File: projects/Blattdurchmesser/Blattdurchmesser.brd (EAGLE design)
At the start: 100 x 80 mm, 14 parts, among them K1 TX2_RELAY", U1 ARDUINOR3-DIMENSION

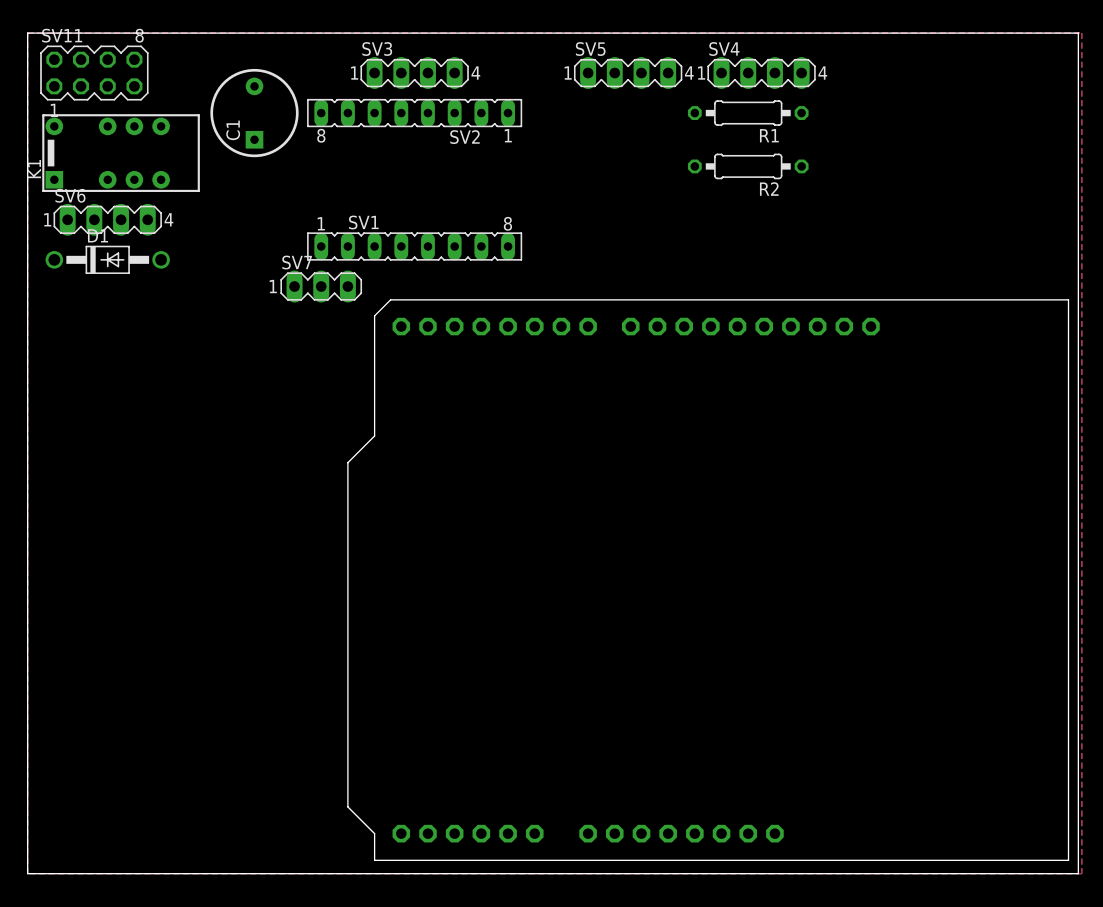
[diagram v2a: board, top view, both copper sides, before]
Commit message: improvement; * replace arduino part/footprint by one that does                not have milling slots              * avoid using a relais as it has disadvantages
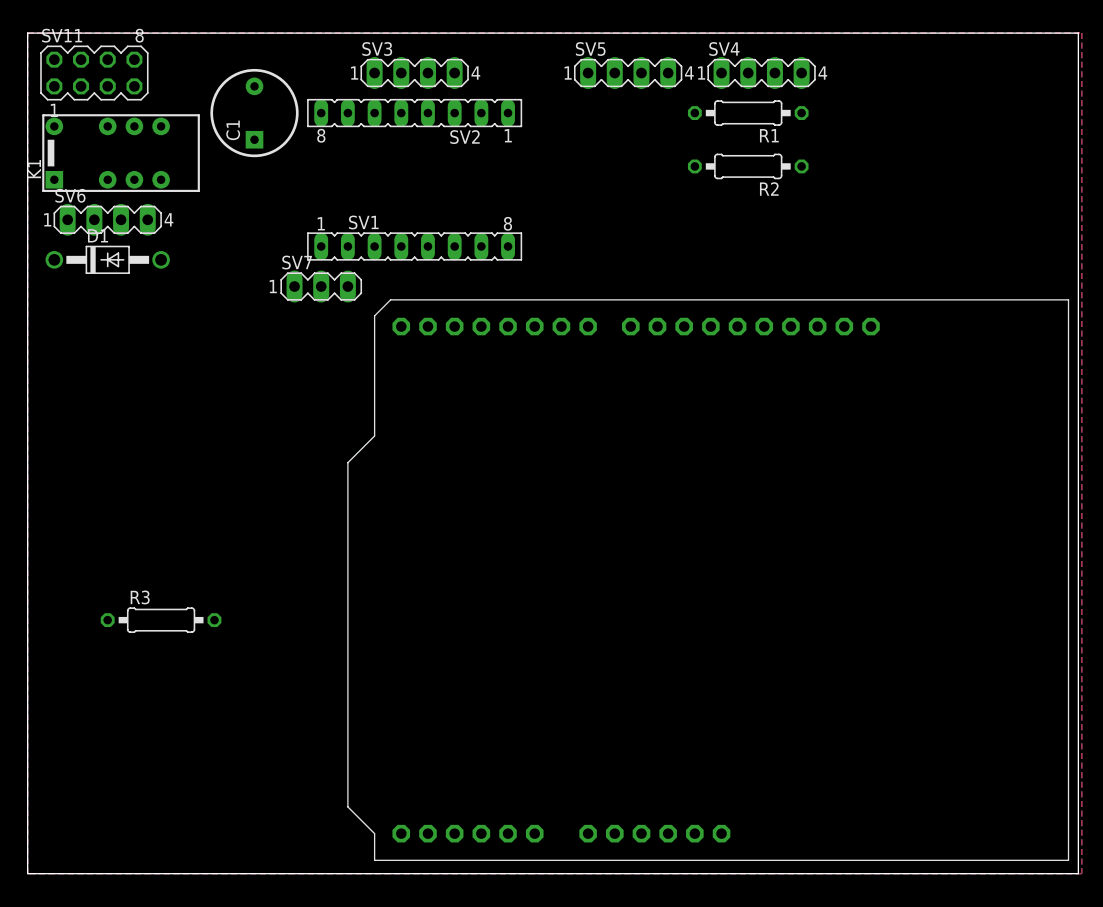
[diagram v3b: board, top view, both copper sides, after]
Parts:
- removed U1: ARDUINOR3-DIMENSION, adafruit:ARDUINOR3
- added Q1: ARDUINOR3-NOIOREF-NOTEXT, adafruit:ARDUINOR3-NOTEXT-NOIOREF
- added R3: ?, rcl:0207/10
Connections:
- removed net N$10: K1.4, SV1.1, SV7.2
- new net N$16: D1.C, K1.1
- new net N$8: D1.A, K1.12
- net +12V: no longer D1.C, K1.1
- net +5V: now also Q1.5V, R3.2; no longer K1.3, U1.5V
- net 3V: now also Q1.3V; no longer U1.3V
- net GND: now also Q1.GND; no longer SV6.1, U1.GND
- net GND1: now also Q1.GND1; no longer U1.GND1
- net GND2: now also Q1.GND2; no longer U1.GND2
- net N$1: now also Q1.D4; no longer U1.D4
- net N$11: now also Q1.D12, SV6.1; no longer D1.A, K1.12, SV6.2
- net N$12: now also Q1.D10; no longer U1.D10
- net N$13: now also Q1.D9; no longer U1.D9
- net N$14: now also R3.1, SV1.1, SV6.2, SV7.2; no longer K1.5, SV7.1, U1.D12
- net N$15: now also Q1.D2; no longer U1.D2
- net N$2: now also Q1.D3; no longer U1.D3
- net N$9: now also Q1.D8; no longer U1.D8
- net VIN: now also Q1.VIN; no longer U1.VIN
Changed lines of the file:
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@@
 </autorouter>
 <elements>
-<element name="U1" library="adafruit" package="ARDUINOR3" value="ARDUINOR3-DIMENSION" x="99.06" y="1.27" rot="MR0"/>
 <element name="K1" library="relay" package="TX2" value="TX2_RELAY&quot;" x="8.89" y="68.58"/>
 <element name="SV1" library="con-lsta" package="FE08" value="" x="36.83" y="59.69">
@@
 <attribute name="MF" value="" x="27.94" y="55.88" size="1.778" layer="27" display="off"/>
 </element>
+<element name="R3" library="rcl" package="0207/10" value="?" x="12.7" y="24.13"/>
+<element name="Q1" library="adafruit" package="ARDUINOR3-NOTEXT-NOIOREF" value="ARDUINOR3-NOIOREF-NOTEXT" x="99.06" y="1.27" rot="MR0"/>
 </elements>
 <signals>
 <signal name="GND">
-<contactref element="U1" pad="GND"/>
 <contactref element="SV2" pad="1"/>
 <contactref element="SV2" pad="7"/>
@@
 <contactref element="SV11" pad="3"/>
 <contactref element="SV11" pad="1"/>
-<contactref element="SV6" pad="1"/>
 <polygon width="0.4064" layer="16">
 <vertex x="0" y="80.01"/>
@@
 <vertex x="0" y="0"/>
 </polygon>
-<wire x1="73.66" y1="76.2" x2="72.644" y2="52.07" width="0" layer="19" extent="1-1"/>
+<contactref element="Q1" pad="GND"/>
 </signal>
 <signal name="VIN">
-<contactref element="U1" pad="VIN"/>
+<contactref element="Q1" pad="VIN"/>
 </signal>
 <signal name="GND1">
-<contactref element="U1" pad="GND1"/>
+<contactref element="Q1" pad="GND1"/>
 </signal>
 <signal name="GND2">
-<contactref element="U1" pad="GND2"/>
+<contactref element="Q1" pad="GND2"/>
 </signal>
 <signal name="3V">
-<contactref element="U1" pad="3V"/>
+<contactref element="Q1" pad="3V"/>
 </signal>
 <signal name="+5V">
 <contactref element="SV2" pad="2"/>
-<contactref element="U1" pad="5V"/>
 <contactref element="SV4" pad="1"/>
 <contactref element="R1" pad="2"/>
 <contactref element="R2" pad="2"/>
-<contactref element="K1" pad="3"/>
 <polygon width="0.4064" layer="1">
 <vertex x="0" y="0"/>
@@
 <vertex x="100.33" y="0"/>
 </polygon>
-<wire x1="63.5" y1="67.31" x2="60.96" y2="3.81" width="0" layer="19" extent="1-1"/>
+<contactref element="R3" pad="2"/>
+<contactref element="Q1" pad="5V"/>
 </signal>
 <signal name="+12V">
 <contactref element="SV2" pad="8"/>
 <contactref element="C1" pad="P"/>
-<contactref element="K1" pad="1"/>
-<contactref element="D1" pad="C"/>
 <wire x1="21.59" y1="69.85" x2="27.94" y2="72.39" width="0" layer="19" extent="1-1"/>
-<wire x1="2.54" y1="66.04" x2="21.59" y2="69.85" width="0" layer="19" extent="1-1"/>
-<wire x1="2.54" y1="58.42" x2="2.54" y2="66.04" width="0" layer="19" extent="1-1"/>
 </signal>
 <signal name="N$3">
@@
 <signal name="N$1">
 <contactref element="SV1" pad="8"/>
-<contactref element="U1" pad="D4"/>
+<contactref element="Q1" pad="D4"/>
 <wire x1="45.72" y1="52.07" x2="45.72" y2="59.69" width="0" layer="19" extent="1-1"/>
 </signal>
 <signal name="N$2">
 <contactref element="SV1" pad="7"/>
-<contactref element="U1" pad="D3"/>
+<contactref element="Q1" pad="D3"/>
 <wire x1="43.18" y1="52.07" x2="43.18" y2="59.69" width="0" layer="19" extent="1-1"/>
 </signal>
@@
 <contactref element="SV4" pad="3"/>
 <contactref element="R2" pad="1"/>
-<contactref element="U1" pad="D8"/>
+<contactref element="Q1" pad="D8"/>
 <wire x1="73.66" y1="67.31" x2="71.12" y2="76.2" width="0" layer="19" extent="1-1"/>
 <wire x1="57.404" y1="52.07" x2="73.66" y2="67.31" width="0" layer="19" extent="1-1"/>
@@
 <signal name="N$12">
 <contactref element="SV5" pad="2"/>
-<contactref element="U1" pad="D10"/>
+<contactref element="Q1" pad="D10"/>
 <wire x1="62.484" y1="52.07" x2="55.88" y2="76.2" width="0" layer="19" extent="1-1"/>
 </signal>
 <signal name="N$13">
 <contactref element="SV5" pad="4"/>
-<contactref element="U1" pad="D9"/>
+<contactref element="Q1" pad="D9"/>
 <wire x1="59.944" y1="52.07" x2="60.96" y2="76.2" width="0" layer="19" extent="1-1"/>
 </signal>
-<signal name="N$11">
+<signal name="N$14">
 <contactref element="SV6" pad="2"/>
-<contactref element="K1" pad="12"/>
-<contactref element="D1" pad="A"/>
-<wire x1="6.35" y1="62.23" x2="2.54" y2="71.12" width="0" layer="19" extent="1-1"/>
-<wire x1="12.7" y1="58.42" x2="6.35" y2="62.23" width="0" layer="19" extent="1-1"/>
-</signal>
-<signal name="N$14">
-<contactref element="U1" pad="D12"/>
-<contactref element="K1" pad="5"/>
-<contactref element="SV7" pad="1"/>
-<wire x1="25.4" y1="55.88" x2="67.564" y2="52.07" width="0" layer="19" extent="1-1"/>
-<wire x1="12.7" y1="66.04" x2="25.4" y2="55.88" width="0" layer="19" extent="1-1"/>
-</signal>
-<signal name="N$10">
 <contactref element="SV1" pad="1"/>
-<contactref element="K1" pad="4"/>
 <contactref element="SV7" pad="2"/>
+<contactref element="R3" pad="1"/>
 <wire x1="27.94" y1="55.88" x2="27.94" y2="59.69" width="0" layer="19" extent="1-1"/>
-<wire x1="10.16" y1="66.04" x2="27.94" y2="59.69" width="0" layer="19" extent="1-1"/>
+<wire x1="6.35" y1="62.23" x2="27.94" y2="59.69" width="0" layer="19" extent="1-1"/>
+<wire x1="7.62" y1="24.13" x2="27.94" y2="55.88" width="0" layer="19" extent="1-1"/>
 </signal>
 <signal name="N$15">
 <contactref element="SV4" pad="2"/>
 <contactref element="R1" pad="1"/>
-<contactref element="U1" pad="D2"/>
+<contactref element="Q1" pad="D2"/>
 <wire x1="73.66" y1="72.39" x2="68.58" y2="76.2" width="0" layer="19" extent="1-1"/>
 <wire x1="40.64" y1="52.07" x2="68.58" y2="76.2" width="0" layer="19" extent="1-1"/>
 </signal>
+<signal name="N$8">
+<contactref element="K1" pad="12"/>
+<contactref element="D1" pad="A"/>
+<wire x1="12.7" y1="58.42" x2="2.54" y2="71.12" width="0" layer="19" extent="1-1"/>
+</signal>
+<signal name="N$16">
+<contactref element="K1" pad="1"/>
+<contactref element="D1" pad="C"/>
+<wire x1="2.54" y1="58.42" x2="2.54" y2="66.04" width="0" layer="19" extent="1-1"/>
+</signal>
+<signal name="N$11">
+<contactref element="SV6" pad="1"/>
+<contactref element="Q1" pad="D12"/>
+<wire x1="3.81" y1="62.23" x2="67.564" y2="52.07" width="0" layer="19" extent="1-1"/>
+</signal>
 </signals>

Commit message: improvement; * pcb routed for 1st time
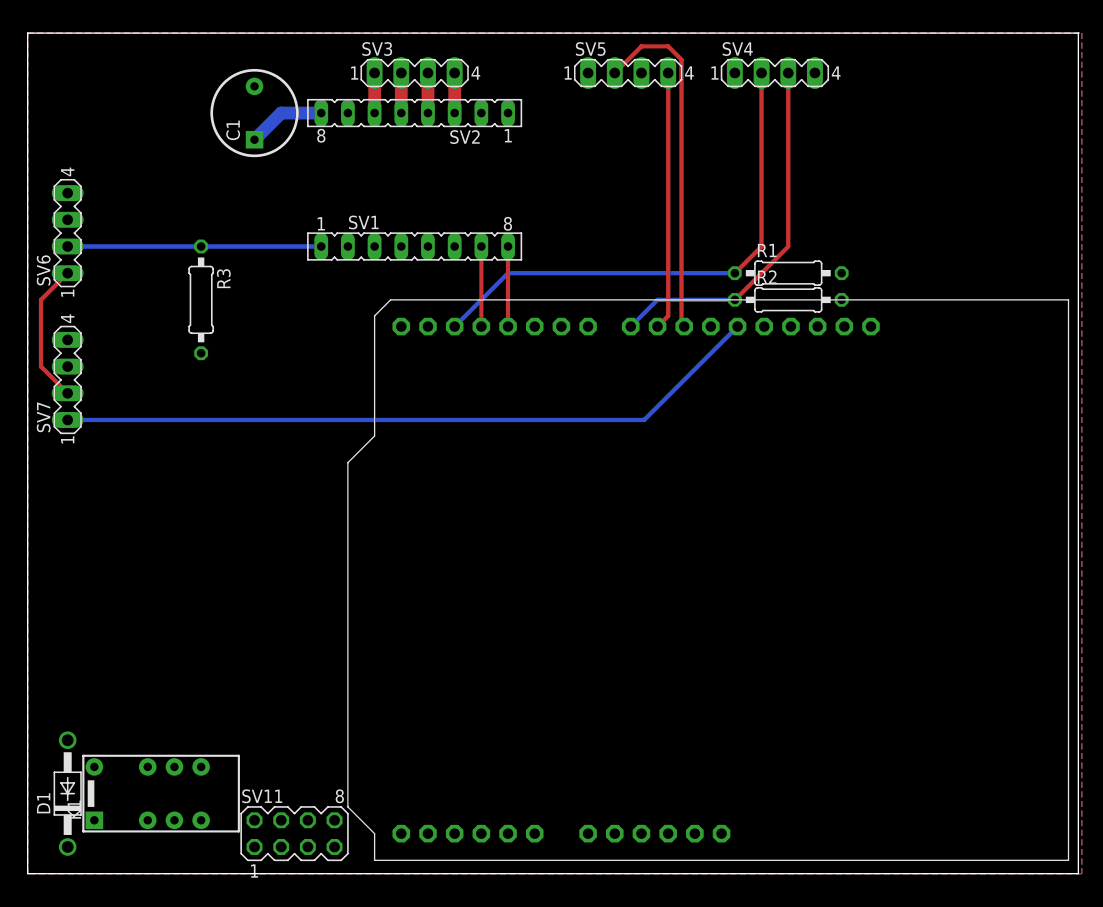
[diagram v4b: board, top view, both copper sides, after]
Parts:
- SV7: device con-lstb:MA03-1 -> con-lstb:MA04-1
- moved SV11 74.9 mm to (25.4, 3.81)
- moved K1 61.1 mm to (12.7, 7.62)
- moved D1 50.9 mm to (3.81, 7.62), turned to 90 degrees
- moved R3 30.7 mm to (16.5, 54.6), turned to 270 degrees
- moved SV7 25.7 mm to (3.81, 47.0), turned to 90 degrees
- moved R1 15.7 mm to (72.4, 57.1), turned to 0 degrees
- moved R2 13.3 mm to (72.4, 54.6), turned to 0 degrees
- moved SV6 4.02 mm to (3.81, 61.0), turned to 90 degrees
- moved SV4 1.27 mm to (71.1, 76.2)
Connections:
- new net N$10: SV6.1, SV7.2
- net N$11: now also SV7.1; no longer SV6.1
- net N$14: no longer SV7.2
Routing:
- net N$11: track 0.00 -> 67.4 mm
- net N$15: track 0.00 -> 48.9 mm
- net N$9: track 0.00 -> 34.7 mm
- net N$12: track 0.00 -> 33.4 mm
- net N$13: track 0.00 -> 24.6 mm
- net N$14: track 0.00 -> 24.1 mm
- net N$10: track 0.00 -> 13.5 mm
- net N$2: track 0.00 -> 7.62 mm
- net N$1: track 0.00 -> 7.62 mm
- net +12V: track 0.00 -> 7.40 mm
- net N$6: track 0.00 -> 3.81 mm
- net N$5: track 0.00 -> 3.81 mm
- net N$4: track 0.00 -> 3.81 mm
- net N$3: track 0.00 -> 3.81 mm

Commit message: improvement; * put everything closer to meet space restrictions              * add 7805 (+5V) voltage regulator (derive from +12V)              * add a wire clamp for +12V power connection
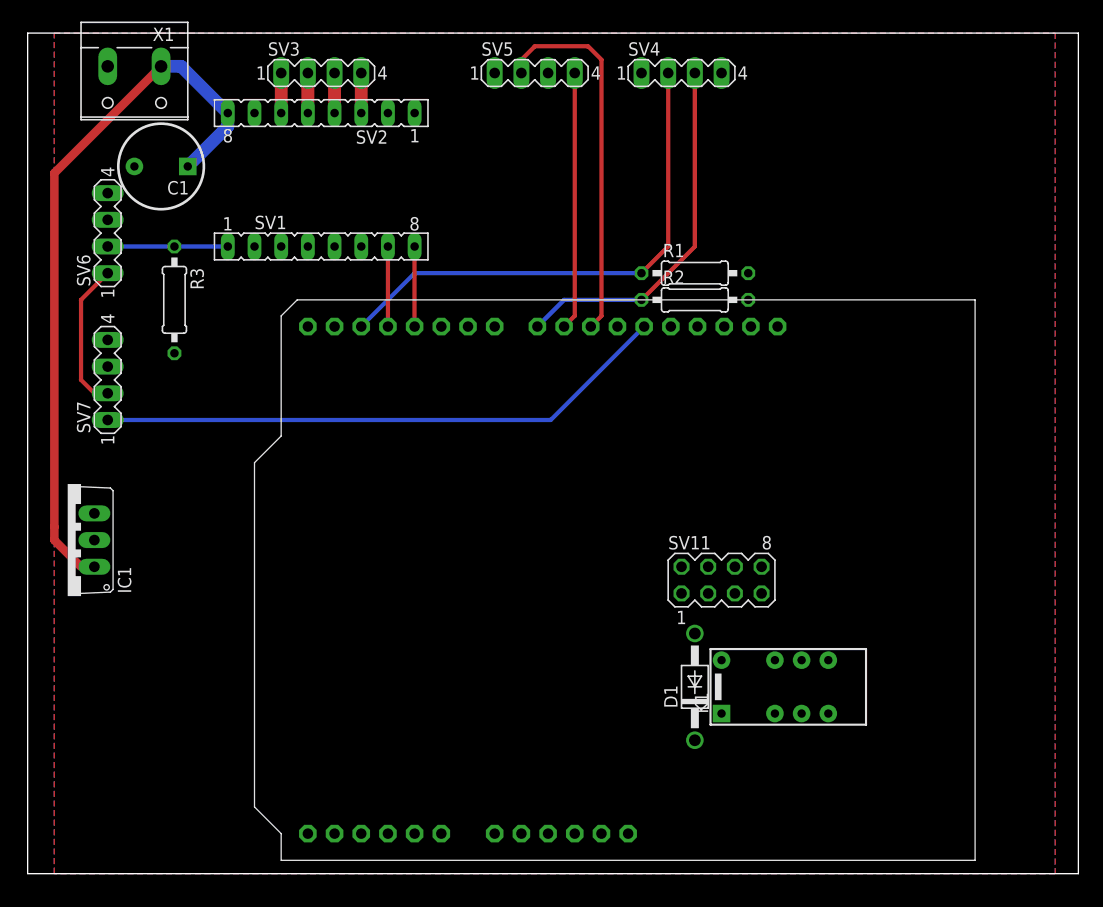
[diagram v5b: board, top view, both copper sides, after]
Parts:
- added IC1: 7805TV, linear:TO220V
- added X1: (no value), con-wago-508:W237-132
- R1, R2: value ? -> 1k
- R3: value ? -> 4.7k
- moved D1 60.5 mm to (63.5, 17.8)
- moved K1 60.5 mm to (72.4, 17.8)
- moved SV11 47.3 mm to (66.0, 27.9)
- moved SV4 8.89 mm to (62.2, 76.2)
- moved Q1 8.89 mm to (90.2, 1.27)
- moved R1 8.89 mm to (63.5, 57.1)
- moved R2 8.89 mm to (63.5, 54.6)
- moved SV5 8.89 mm to (48.3, 76.2)
- moved SV1 8.89 mm to (27.9, 59.7)
- moved SV2 8.89 mm to (27.9, 72.4)
- moved SV3 8.89 mm to (27.9, 76.2)
- moved C1 8.52 mm to (14.0, 67.3), turned to 180 degrees
- moved SV6 3.81 mm to (7.62, 61.0)
- moved SV7 3.81 mm to (7.62, 47.0)
- moved R3 2.54 mm to (14.0, 54.6)
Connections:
- net +12V: now also IC1.1, X1.1
- net +5V: now also IC1.3
- net GND: now also IC1.2, X1.2
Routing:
- net +12V: track 7.40 -> 69.0 mm
- net N$14: track 24.1 -> 11.4 mm
- net N$11: track 67.4 -> 54.7 mm
- net N$12: track 33.4 -> 35.8 mm
- net N$10: track 13.5 -> 14.3 mm
